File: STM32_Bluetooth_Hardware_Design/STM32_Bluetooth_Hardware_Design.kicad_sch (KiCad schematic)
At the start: 21 parts, among them U1 STM32WB55CEUx, X1 32kHz, X2 32MHz

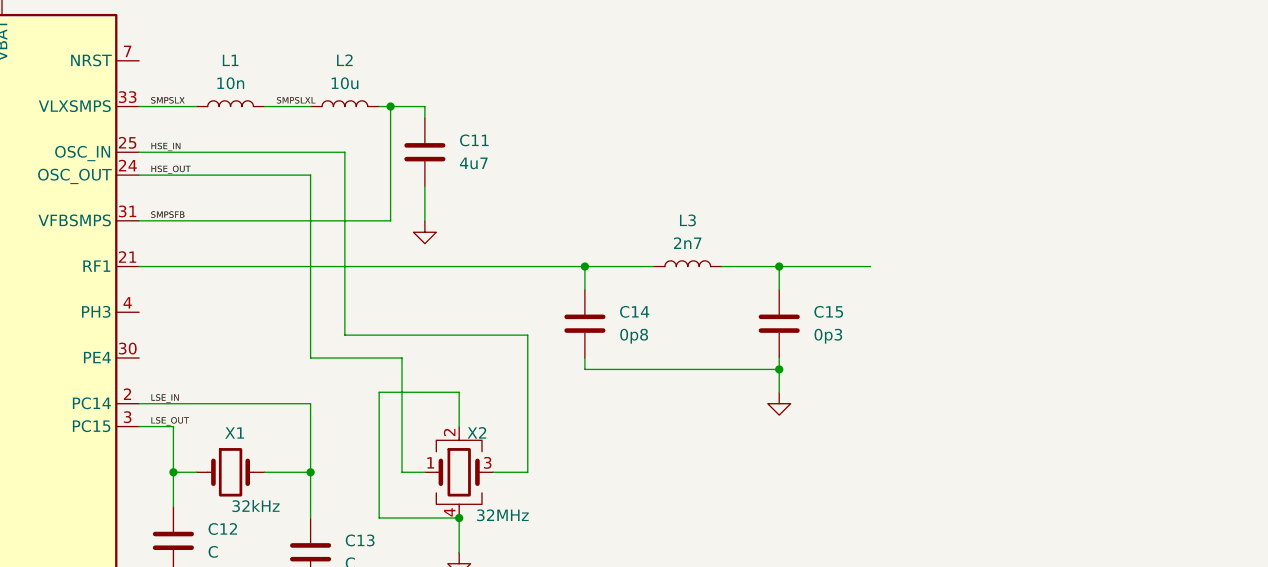
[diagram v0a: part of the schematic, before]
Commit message: LPF and RF Antenna
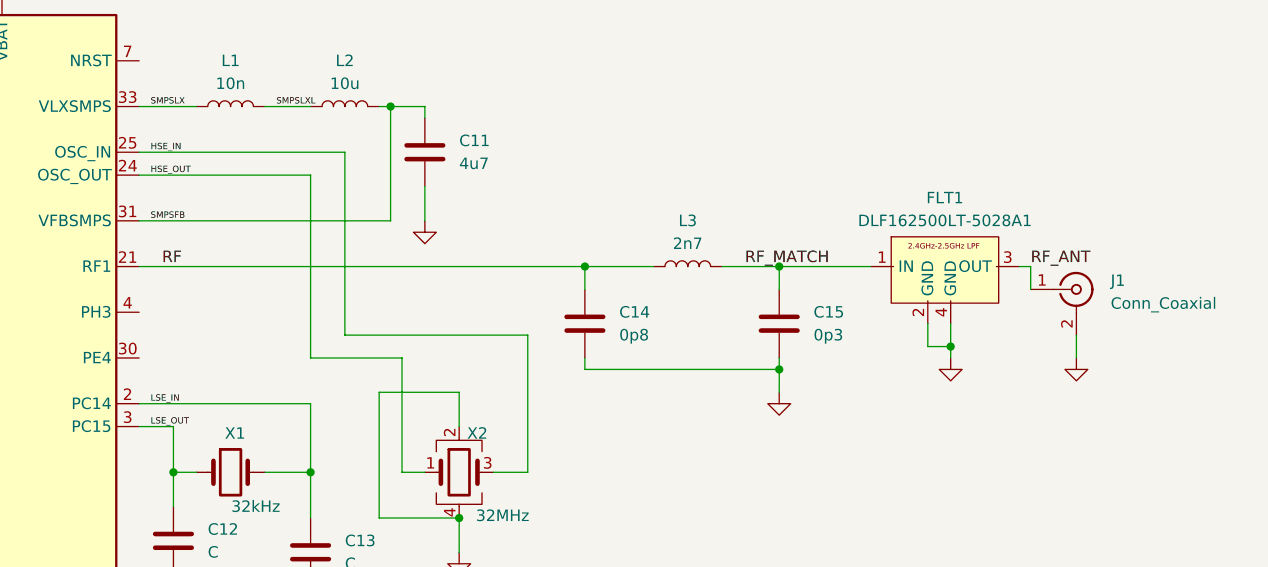
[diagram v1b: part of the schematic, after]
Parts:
- added FLT1: DLF162500LT-5028A1, My_Lib:DLF162500LT-5028A1, symbol My_Lib:DLF162500LT-5028A1
- added J1: Conn_Coaxial, symbol Connector:Conn_Coaxial
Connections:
- net GND: now also FLT1.2 (GND), FLT1.4 (GND), J1.2 (Ext)
- net RF: now reaches C14.1, L3.1, U1.21 (RF1)
- net RF_MATCH: now reaches C15.1, L3.2
- net RF_MATCH: now also FLT1.1 (IN)
- new net RF_ANT: FLT1.3 (OUT), J1.1 (In)

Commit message: STM32 UART
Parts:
- added C16, C17: 100n, symbol Device:C
- added C18, C19: 4u7, symbol Device:C
- added D1: LED, symbol Device:LED
- added J2: Conn_ARM_SWD_TagConnect_TC2030, Connector:Tag-Connect_TC2030-IDC-FP_2x03_P1.27mm_Vertical, symbol Connector:Conn_ARM_SWD_TagConnect_TC2030
- added J3: USB_C_Receptacle_USB2.0_16P, symbol Connector:USB_C_Receptacle_USB2.0_16P
- added J4: Conn_01x04, symbol Connector_Generic:Conn_01x04
- added R1, R3, R4: 5k1, symbol Device:R
- added R2: 100R, symbol Device:R
- added R5, R6, R7: 220R, symbol Device:R
- added SW1: SW_Push, symbol Switch:SW_Push
- added U2: USBLC6-2SC6, Package_TO_SOT_SMD:SOT-23-6, symbol Power_Protection:USBLC6-2SC6
- added U3: MIC5365-3.3YD5, Package_TO_SOT_SMD:SOT-23-5, symbol Regulator_Linear:MIC5365-3.3YD5
- X1: value 32kHz -> 32kHz768
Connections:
- net +3V3: now also C18.1, J2.1 (VCC), J4.4 (Pin_4), SW1.2, U3.5 (VOUT)
- net GND: now also C16.2, C17.2, C18.2, C19.2, J2.5 (GND), J3.A1 (GND), J3.A12 (GND), J3.B1 (GND), J3.B12 (GND), J3.S1 (SHIELD), J4.1 (Pin_1), R1.2, R3.2, R4.2, R7.1, U2.2 (GND), U3.2 (GND)
- net UART_TX: now reaches U1.11 (PA2)
- net UART_TX: now also R5.2
- net UART_RX: now reaches U1.12 (PA3)
- net UART_RX: now also R6.2
- net LED_A: now reaches U1.16 (PA7)
- net LED_A: now also D1.2 (A)
- net USB_D-: now reaches U1.37 (PA11)
- net USB_D-: now also U2.6 (I/O1)
- net USB_D+: now reaches U1.38 (PA12)
- net USB_D+: now also U2.4 (I/O2)
- net SWD_DIO: now reaches U1.39 (PA13)
- net SWD_DIO: now also J2.2 (SWDIO)
- net BOOT0: now reaches U1.4 (PH3)
- net BOOT0: now also C17.1, R1.1, R2.1
- net SWD_CLK: now reaches U1.41 (PA14)
- net SWD_CLK: now also J2.4 (SWCLK)
- net SWD_TRC: now reaches U1.43 (PB3)
- net SWD_TRC: now also J2.6 (SWO)
- net SWD_NRST: now reaches U1.7 (NRST)
- net SWD_NRST: now also C16.1, J2.3 (~{RESET})
- new net: R2.2, SW1.1
- new net: J3.A5 (CC1), R3.1
- new net: J3.B5 (CC2), R4.1
- new net: J3.A7 (D-), J3.B7 (D-), U2.1 (I/O1)
- new net: J3.A6 (D+), J3.B6 (D+), U2.3 (I/O2)
- new net +5V: C19.1, J3.A4 (VBUS), J3.A9 (VBUS), J3.B4 (VBUS), J3.B9 (VBUS), U2.5 (VBUS), U3.1 (VIN), U3.3 (EN)
- new net LED_K: D1.1 (K), R7.2
- new net UART_RXC: J4.2 (Pin_2), R6.1
- new net UART_TXC: J4.3 (Pin_3), R5.1
- no-connect marks 0 -> 21
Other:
- note added: "(3.3-1.8)/220 = 7 mA"
- note added: "5v from usb"
- note added: "LSE (32.768kHz) & HSE (32MHz) Crystals"
- note added: "STM32WB55 MCU"
- note added: "STM32_Bluetooth_Hardware_Design"
- note added: "Tag Connect SWD Header"
- note added: "UART_Header"
- note added: "USB-C Connector"
- note added: "Voltage LDO Regulator from 5v to 3.3v"

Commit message: STM32 UART
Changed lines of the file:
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@@
 			(font
 				(size 4 4)
-				(thickness 0.4)
-				(bold yes)
-				(color 53 20 255 1)
+				(thickness 0.5)
+				(color 0 0 0 1)
 			)
 		)

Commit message: STM32 UART
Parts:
- C1, C10, C14, C15, C16, C17, C2, C3, C4, C5, C6, C9: footprint (none) -> Capacitor_SMD:C_0402_1005Metric
- C11, C18, C19, C7, C8: footprint (none) -> Capacitor_SMD:C_0603_1608Metric
- C12, C13: value C -> 10p; footprint (none) -> Capacitor_SMD:C_0402_1005Metric
- D1: footprint (none) -> LED_SMD:LED_0402_1005Metric
- J1: footprint (none) -> Connector_Coaxial:U.FL_Hirose_U.FL-R-SMT-1_Vertical
- J3: footprint (none) -> Connector_USB:USB_C_Receptacle_GCT_USB4105-xx-A_16P_TopMnt_Horizontal
- J4: footprint (none) -> Connector_Molex:Molex_PicoBlade_53048-0410_1x04_P1.25mm_Horizontal
- L1, L3: footprint (none) -> Inductor_SMD:L_0402_1005Metric
- L2: footprint (none) -> Inductor_SMD:L_0805_2012Metric
- R1, R2, R3, R4, R5, R6, R7: footprint (none) -> Resistor_SMD:R_0402_1005Metric
- SW1: footprint (none) -> Button_Switch_SMD:SW_SPST_CK_RS282G05A3
- X1: footprint (none) -> Crystal:Crystal_SMD_2012-2Pin_2.0x1.2mm
- X2: footprint (none) -> Crystal:Crystal_SMD_2016-4Pin_2.0x1.6mm
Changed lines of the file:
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@@
 			)
 		)
-		(property "Footprint" ""
+		(property "Footprint" "Resistor_SMD:R_0402_1005Metric"
 			(at 223.012 152.4 90)
 			(effects
@@
 			)
 		)
-		(property "Footprint" ""
+		(property "Footprint" "Button_Switch_SMD:SW_SPST_CK_RS282G05A3"
 			(at 259.08 140.97 0)
 			(effects
@@
 			)
 		)
-		(property "Footprint" ""
+		(property "Footprint" "Resistor_SMD:R_0402_1005Metric"
 			(at 107.95 91.948 90)
 			(effects
@@
 			)
 		)
-		(property "Footprint" ""
+		(property "Footprint" "Connector_Molex:Molex_PicoBlade_53048-0410_1x04_P1.25mm_Horizontal"
 			(at 88.9 90.17 0)
 			(effects
@@
 			)
 		)
-		(property "Footprint" ""
+		(property "Footprint" "Capacitor_SMD:C_0402_1005Metric"
 			(at 113.9952 71.12 0)
 			(effects
@@
 			)
 		)
-		(property "Footprint" ""
+		(property "Footprint" "Capacitor_SMD:C_0402_1005Metric"
 			(at 122.8852 71.12 0)
 			(effects
@@
 			)
 		)
-		(property "Footprint" ""
+		(property "Footprint" "Inductor_SMD:L_0402_1005Metric"
 			(at 232.41 105.41 0)
 			(effects
@@
 			)
 		)
-		(property "Footprint" ""
+		(property "Footprint" "LED_SMD:LED_0402_1005Metric"
 			(at 118.11 100.33 0)
 			(effects
@@
 			)
 		)
-		(property "Footprint" ""
+		(property "Footprint" "Capacitor_SMD:C_0402_1005Metric"
 			(at 135.5852 43.18 0)
 			(effects
@@
 			)
 		)
-		(property "Footprint" ""
+		(property "Footprint" "Capacitor_SMD:C_0402_1005Metric"
 			(at 74.6252 71.12 0)
 			(effects
@@
 			)
 		)
-		(property "Footprint" ""
+		(property "Footprint" "Capacitor_SMD:C_0402_1005Metric"
 			(at 152.7048 43.18 0)
 			(effects
@@
 			)
 		)
-		(property "Footprint" ""
+		(property "Footprint" "Capacitor_SMD:C_0603_1608Metric"
 			(at 64.4652 71.12 0)
 			(effects
@@
 			)
 		)
-		(property "Footprint" ""
+		(property "Footprint" "Capacitor_SMD:C_0402_1005Metric"
 			(at 84.7852 71.12 0)
 			(effects
@@
 			)
 		)
-		(property "Footprint" ""
+		(property "Footprint" "Crystal:Crystal_SMD_2012-2Pin_2.0x1.2mm"
 			(at 181.61 128.27 0)
 			(effects
@@
 			)
 		)
-		(property "Footprint" ""
+		(property "Footprint" "Capacitor_SMD:C_0603_1608Metric"
 			(at 125.4252 43.18 0)
 			(effects
@@
 			)
 		)
-		(property "Footprint" ""
+		(property "Footprint" "Capacitor_SMD:C_0402_1005Metric"
 			(at 243.5352 115.57 0)
 			(effects
@@
 			)
 		)
-		(property "Footprint" ""
+		(property "Footprint" "Inductor_SMD:L_0402_1005Metric"
 			(at 181.61 87.63 0)
 			(effects
@@
 			)
 		)
-		(property "Footprint" ""
+		(property "Footprint" "Crystal:Crystal_SMD_2016-4Pin_2.0x1.6mm"
 			(at 207.01 128.27 0)
 			(effects
@@
 			)
 		)
-		(property "Footprint" ""
+		(property "Footprint" "Resistor_SMD:R_0402_1005Metric"
 			(at 60.452 128.27 90)
 			(effects
@@
 			)
 		)
-		(property "Footprint" ""
+		(property "Footprint" "Resistor_SMD:R_0402_1005Metric"
 			(at 55.372 128.27 90)
 			(effects
@@
 			)
 		)
-		(property "Footprint" ""
+		(property "Footprint" "Capacitor_SMD:C_0603_1608Metric"
 			(at 204.1652 96.52 0)
 			(effects
@@
 			)
 		)
-		(property "Footprint" ""
+		(property "Footprint" "Resistor_SMD:R_0402_1005Metric"
 			(at 109.22 102.108 90)
 			(effects
@@
 			)
 		)
-		(property "Footprint" ""
+		(property "Footprint" "Connector_Coaxial:U.FL_Hirose_U.FL-R-SMT-1_Vertical"
 			(at 275.59 107.95 0)
 			(effects
@@
 			)
 		)
-		(property "Footprint" ""
+		(property "Footprint" "Inductor_SMD:L_0805_2012Metric"
 			(at 194.31 87.63 0)
 			(effects
@@
 			)
 		)
-		(property "Footprint" ""
+		(property "Footprint" "Resistor_SMD:R_0402_1005Metric"
 			(at 246.38 147.828 90)
 			(effects
@@
 			)
 		)
-		(property "Footprint" ""
+		(property "Footprint" "Resistor_SMD:R_0402_1005Metric"
 			(at 107.95 89.408 90)
 			(effects
@@
 			)
 		)
-		(property "Value" "C"
-			(at 171.196 136.652 0)
+		(property "Value" "10p"
+			(at 170.18 137.922 0)
 			(effects
 				(font
@@
 			)
 		)
-		(property "Footprint" ""
+		(property "Footprint" "Capacitor_SMD:C_0402_1005Metric"
 			(at 176.2252 139.7 0)
 			(effects
@@
 			)
 		)
-		(property "Footprint" ""
+		(property "Footprint" "Capacitor_SMD:C_0603_1608Metric"
 			(at 75.8952 33.02 0)
 			(effects
@@
 			)
 		)
-		(property "Footprint" ""
+		(property "Footprint" "Capacitor_SMD:C_0603_1608Metric"
 			(at 39.0652 34.29 0)
 			(effects
@@
 			)
 		)
-		(property "Footprint" ""
+		(property "Footprint" "Capacitor_SMD:C_0402_1005Metric"
 			(at 235.9152 156.21 0)
 			(effects
@@
 			)
 		)
-		(property "Value" "C"
-			(at 185.928 137.922 0)
+		(property "Value" "10p"
+			(at 184.912 138.684 0)
 			(effects
 				(font
@@
 			)
 		)
-		(property "Footprint" ""
+		(property "Footprint" "Capacitor_SMD:C_0402_1005Metric"
 			(at 191.4652 140.97 0)
 			(effects
@@
 			)
 		)
-		(property "Footprint" ""
+		(property "Footprint" "Capacitor_SMD:C_0402_1005Metric"
 			(at 209.2452 82.55 0)
 			(effects
@@
 			)
 		)
-		(property "Footprint" ""
+		(property "Footprint" "Capacitor_SMD:C_0402_1005Metric"
 			(at 96.2152 71.12 0)
 			(effects
@@
 			)
 		)
-		(property "Footprint" ""
+		(property "Footprint" "Capacitor_SMD:C_0402_1005Metric"
 			(at 106.3752 71.12 0)
 			(effects
@@
 			)
 		)
-		(property "Footprint" ""
+		(property "Footprint" "Connector_USB:USB_C_Receptacle_GCT_USB4105-xx-A_16P_TopMnt_Horizontal"
 			(at 38.1 102.87 0)
 			(effects
@@
 			)
 		)
-		(property "Footprint" ""
+		(property "Footprint" "Capacitor_SMD:C_0402_1005Metric"
 			(at 221.9452 115.57 0)
 			(effects
